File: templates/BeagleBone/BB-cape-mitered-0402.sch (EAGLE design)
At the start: 14 parts, among them IC8 EEPROM-I2CSMD

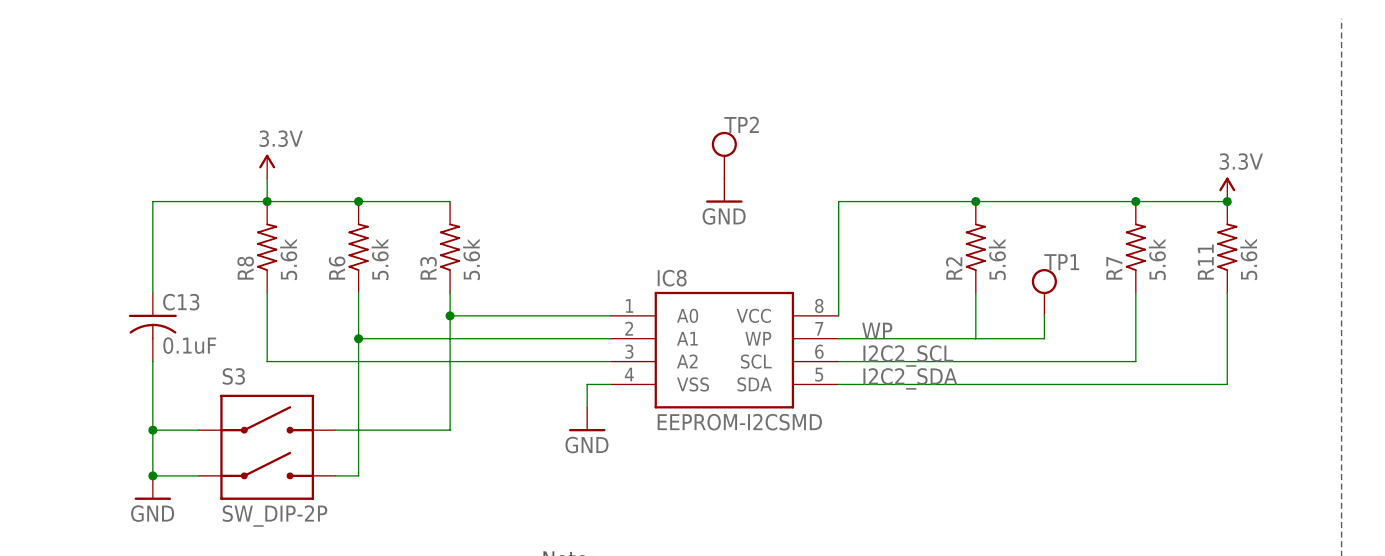
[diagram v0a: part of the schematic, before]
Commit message: renumbered components on templates
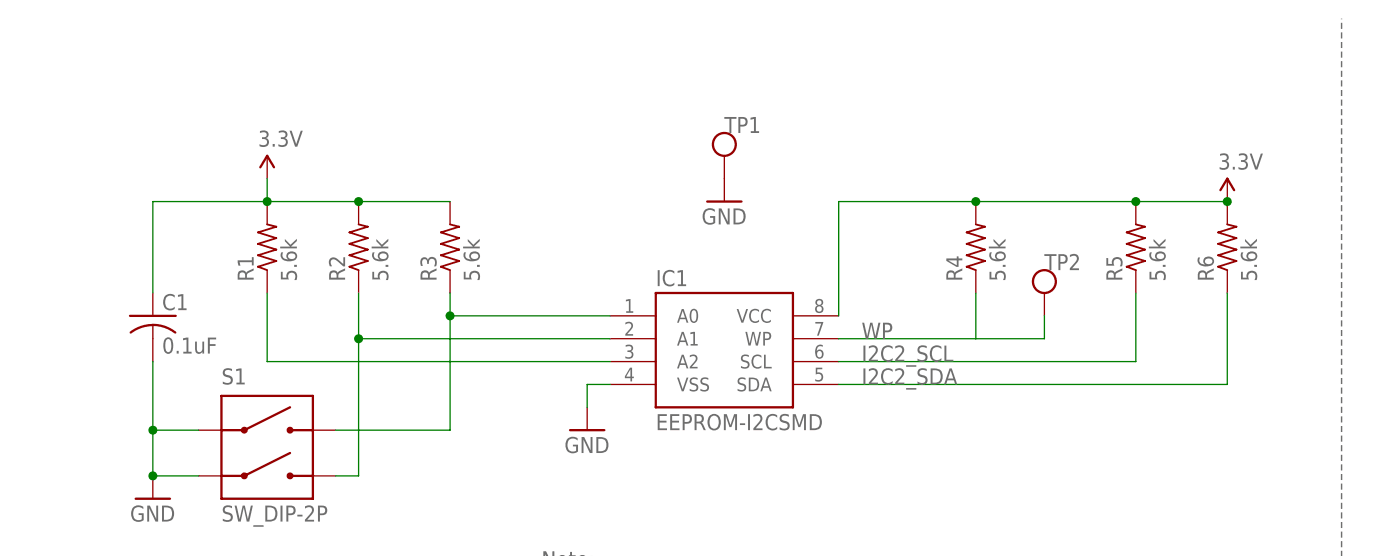
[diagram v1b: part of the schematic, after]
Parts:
- removed R11: 5.6k, logic-supply:R0402
- added R4: 5.6k, logic-supply:R0402
- TP1: BOM (none) -> EXCLUDE
- TP2: BOM EXCLUDE -> (none)
- renumbered C13 to C1, IC8 to IC1, R7 to R5, R8 to R1, S3 to S1
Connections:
- net 3.3V: now also R4.2; no longer R11.2
- net GND: now also TP1.P$1; no longer TP2.P$1
- net I2C2_SDA: now also R6.1; no longer R11.1
- net N$14: now also R2.1; no longer R6.1
- net WP: now also R4.1, TP2.P$1; no longer R2.1, TP1.P$1
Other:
- moved on the sheet: R2, R6, TP1, TP2
